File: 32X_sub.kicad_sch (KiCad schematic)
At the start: 98 parts, among them IC511 315-5684, IC512 315-5788, IC515 74HC74, IC516 74LS00, T520 TestPoint, T526 TestPoint, T527 TestPoint, T528 TestPoint, T547 TestPoint, T548 TestPoint, T555 TestPoint, T599 AS, X501 *3

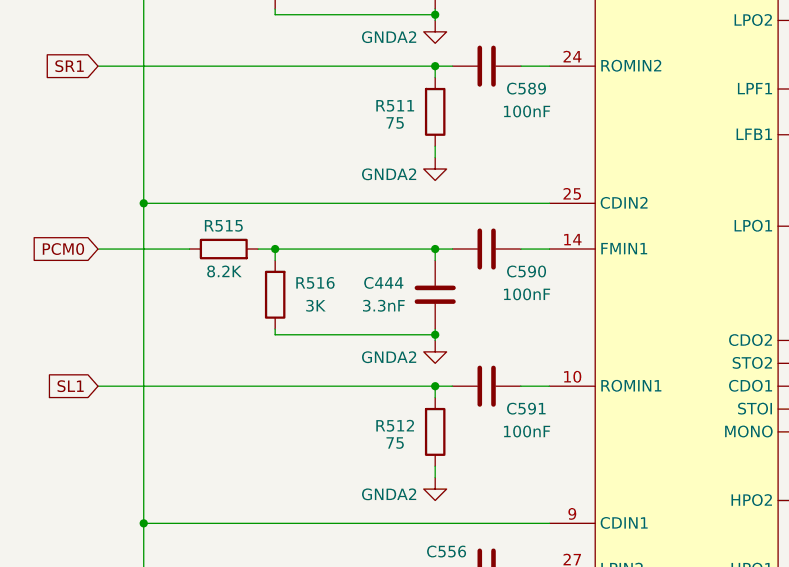
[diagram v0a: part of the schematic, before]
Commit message: BOM/footprint tweaks/corrections.
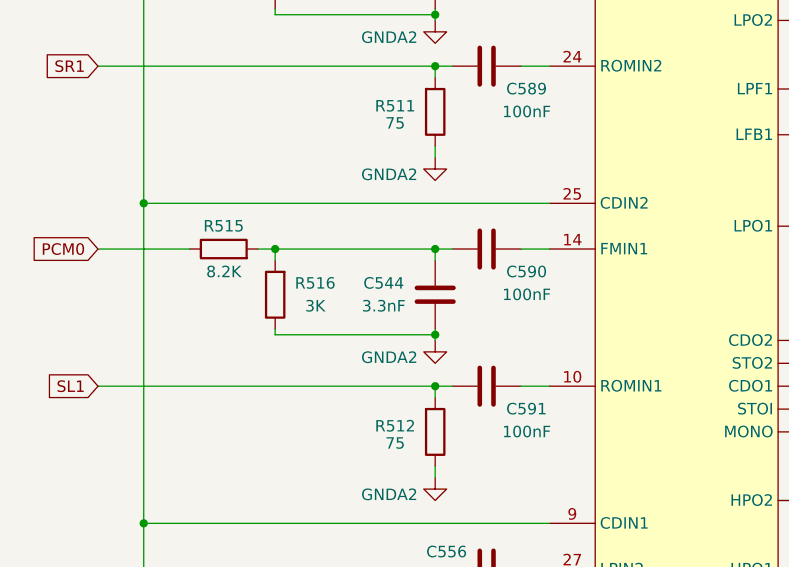
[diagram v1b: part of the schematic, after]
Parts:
- renumbered C444 to C544
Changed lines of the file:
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@@
   (symbol (lib_id "Device:C") (at 91.44 78.74 0) (mirror y) (unit 1)
     (in_bom yes) (on_board yes) (dnp no)
-    (property "Reference" "C444" (at 85.725 77.47 0)
+    (property "Reference" "C544" (at 85.725 77.47 0)
       (effects (font (size 1.27 1.27)))
     )
@@
       (project "Neptune"
         (path "/bcc23b51-b742-4ae5-9dd6-d96a24058944/edde10e2-ce08-4180-9fbe-ab298dfbfa4c"
-          (reference "C444") (unit 1)
+          (reference "C544") (unit 1)
         )
       )

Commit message: General tweaks, add some DigiKey part numbers.
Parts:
- CE17: DigiKey (none) -> 493-13447-1-ND
- R511, R512, R544: DigiKey (none) -> P75.0CCT-ND
- R525: DigiKey (none) -> P2.20KCCT-ND
- R826, R827, R828: DigiKey (none) -> P5.62KCCT-ND
- R829, R830, R831: DigiKey (none) -> P1.00KCCT-ND

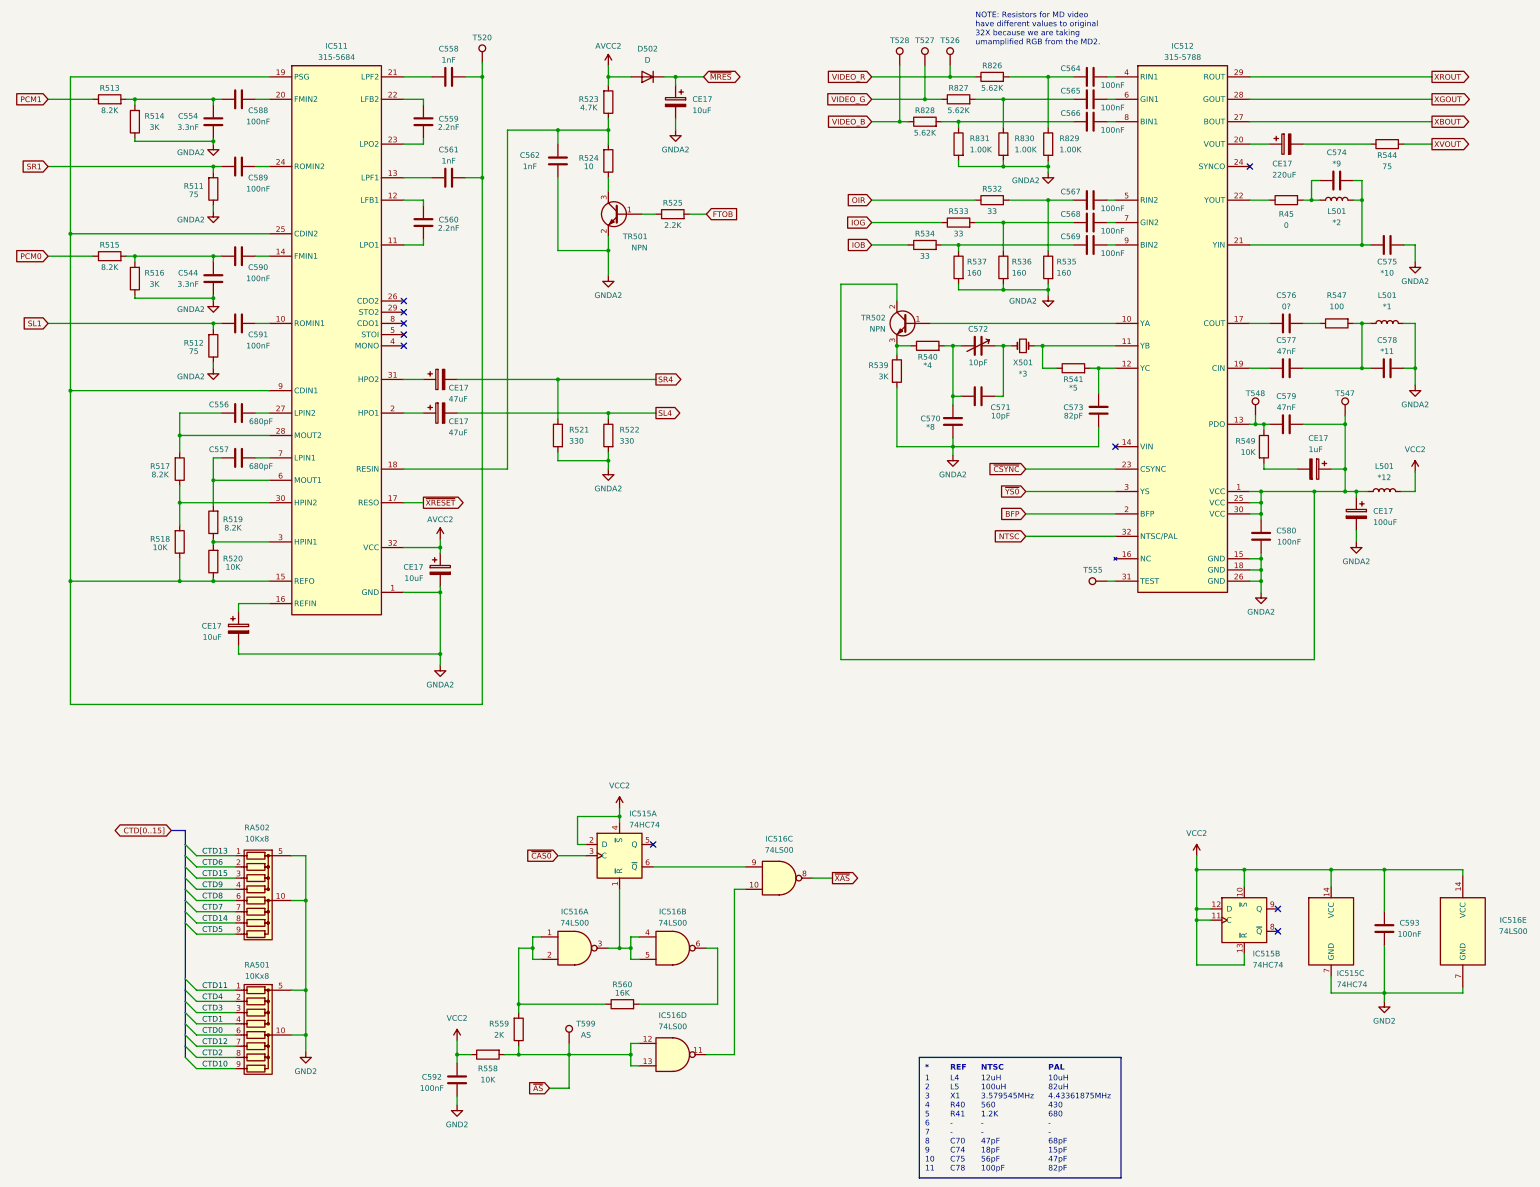
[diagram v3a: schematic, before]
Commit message: Apply fixes for issues found on prototype board.
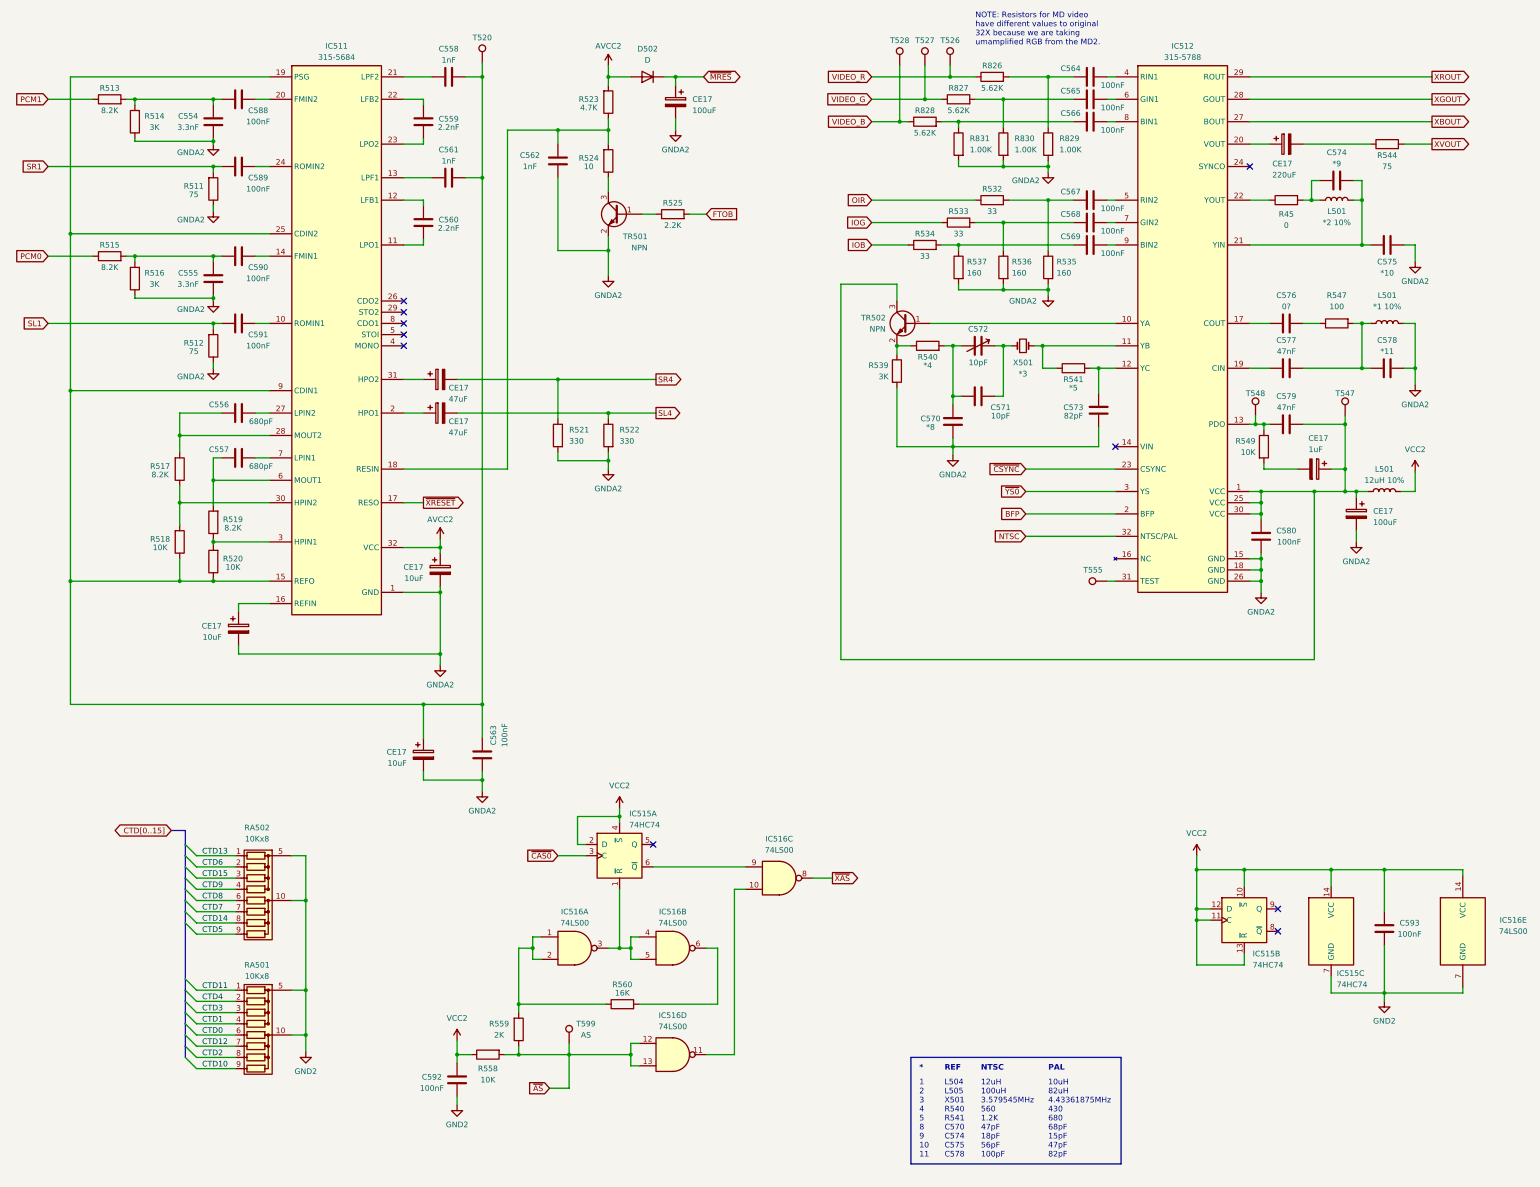
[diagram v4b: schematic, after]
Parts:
- added C563: 100nF, Capacitor_SMD:C_0805_2012Metric, symbol Device:C
- added CE17: 10uF, Capacitor_THT:CP_Radial_D5.0mm_P2.50mm, symbol Device:C_Polarized
- CE17: value 10uF -> 100uF
- L501: value *2 -> *2 10%; footprint Inductor_SMD:L_0805_2012Metric -> Inductor_SMD:L_1206_3216Metric
- L501: value *12 -> 12uH 10%; footprint Inductor_SMD:L_0805_2012Metric -> Inductor_SMD:L_1206_3216Metric
- L501: value *1 -> *1 10%; footprint Inductor_SMD:L_0805_2012Metric -> Inductor_SMD:L_1206_3216Metric
- TR502: symbol Device:Q_NPN_BCE -> Device:Q_NPN_BEC
- renumbered C544 to C555
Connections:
- net GNDA2: now also C563.1, CE17.2
- net at C558.2, C561.2, IC511.15 (REFO)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: now also C563.2, CE17.1
- net at C579.2, C580.2, CE17.1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: now also TR502.3 (C); no longer TR502.2 (C)
- net at R539.1, R540.1: now also TR502.2 (E); no longer TR502.3 (E)
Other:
- note added: "1 2 3 4 5 8 9 10 11"
- note added: "10uH 82uH 4.43361875MHz 430 680 68pF 15pF 47pF 82pF"
- note added: "12uH 100uH 3.579545MHz 560 1.2K 47pF 18pF 56pF 100pF"
- note added: "L504 L505 X501 R540 R541 C570 C574 C575 C578"
- note removed: "1 2 3 4 5 6 7 8 9 10 11"
- note removed: "10uH 82uH 4.43361875MHz 430 680 - - 68pF 15pF 47pF 82pF"
- note removed: "12uH 100uH 3.579545MHz 560 1.2K - - 47pF 18pF 56pF 100pF"
- note removed: "L4 L5 X1 R40 R41 - - C70 C74 C75 C78"

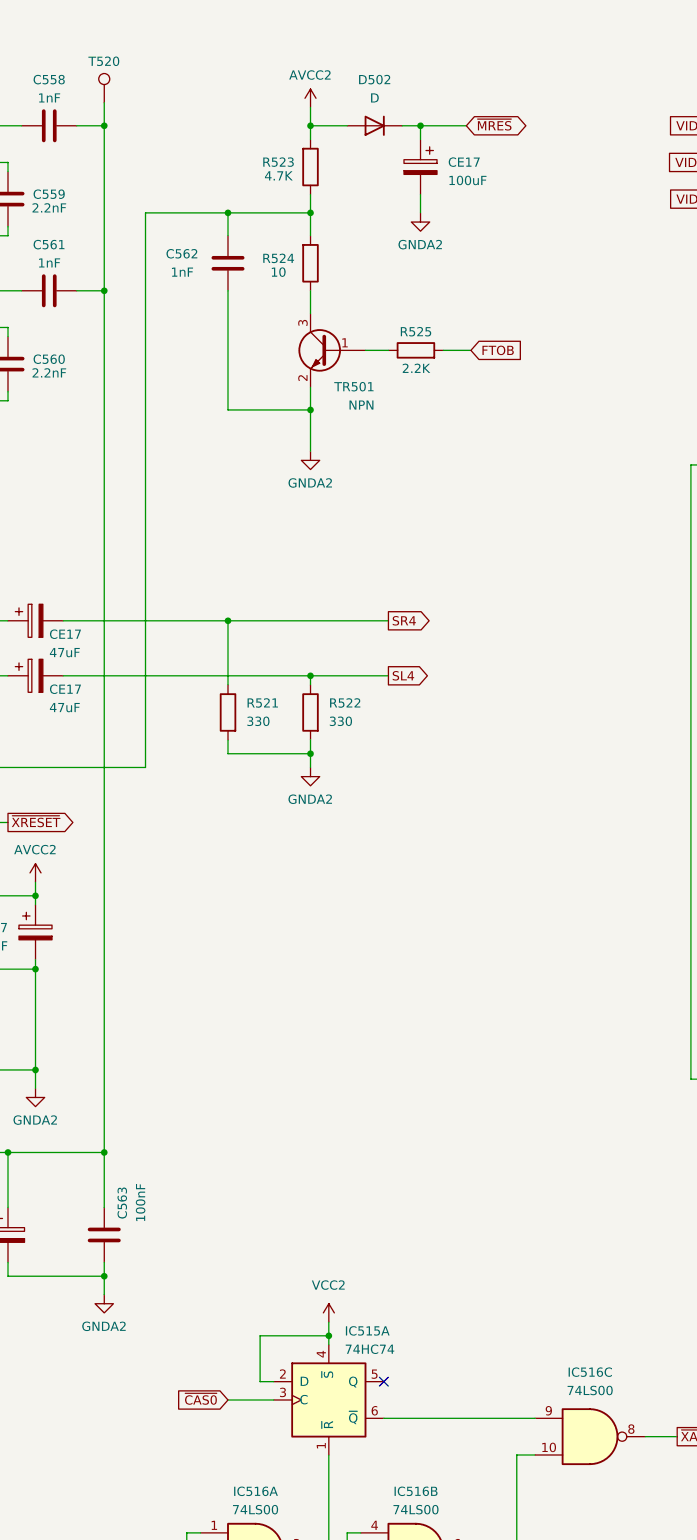
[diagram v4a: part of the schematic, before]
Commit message: Check through 32X VA0/VA1 differences/bodges.
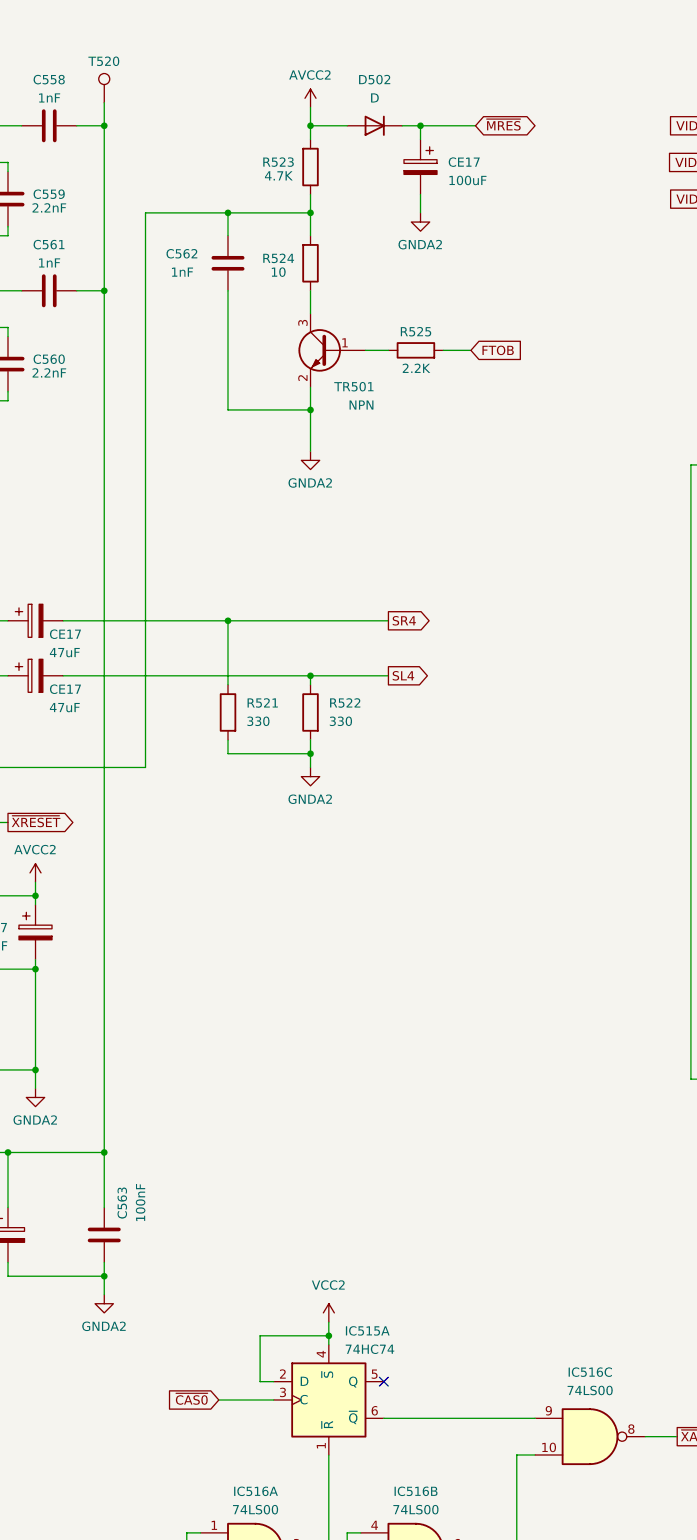
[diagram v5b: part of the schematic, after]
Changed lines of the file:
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@@
+    (stroke (width 0) (type default))
+  )
+  (wire (pts (xy 196.215 33.02) (xy 203.835 33.02))
     (stroke (width 0) (type default))
   )
@@
     (stroke (width 0) (type default))
   )
-  (wire (pts (xy 196.215 33.02) (xy 202.565 33.02))
-    (stroke (width 0) (type default))
-  )
   (wire (pts (xy 279.4 99.06) (xy 282.575 99.06))
     (stroke (width 0) (type default))
@@
     (stroke (width 0) (type default))
   )
+  (wire (pts (xy 196.215 42.545) (xy 196.215 45.085))
+    (stroke (width 0) (type default))
+  )
   (wire (pts (xy 356.87 240.665) (xy 344.805 240.665))
     (stroke (width 0) (type default))
@@
     (stroke (width 0) (type default))
   )
-  (wire (pts (xy 169.545 209.55) (xy 175.895 209.55))
-    (stroke (width 0) (type default))
-  )
   (wire (pts (xy 277.495 93.98) (xy 279.4 93.98))
     (stroke (width 0) (type default))
@@
     (stroke (width 0) (type default))
   )
-  (wire (pts (xy 196.215 42.545) (xy 196.215 45.085))
-    (stroke (width 0) (type default))
-  )
   (wire (pts (xy 100.965 38.1) (xy 104.14 38.1))
     (stroke (width 0) (type default))
@@
   )
   (wire (pts (xy 270.51 66.04) (xy 270.51 72.39))
+    (stroke (width 0) (type default))
+  )
+  (wire (pts (xy 168.275 209.55) (xy 175.895 209.55))
     (stroke (width 0) (type default))
   )
@@
     )
   )
-  (global_label "~{CAS0}" (shape input) (at 169.545 209.55 180) (fields_autoplaced)
-    (effects (font (size 1.27 1.27)) (justify right))
-    (property "Intersheetrefs" "${INTERSHEET_REFS}" (at 161.7822 209.55 0)
+  (global_label "~{CAS0}" (shape input) (at 168.275 209.55 180) (fields_autoplaced)
+    (effects (font (size 1.27 1.27)) (justify right))
+    (property "Intersheetrefs" "${INTERSHEET_REFS}" (at 160.5122 209.55 0)
       (effects (font (size 1.27 1.27)) (justify right) hide)
     )
@@
     )
   )
-  (global_label "~{MRES}" (shape bidirectional) (at 202.565 33.02 0) (fields_autoplaced)
+  (global_label "~{MRES}" (shape bidirectional) (at 203.835 33.02 0) (fields_autoplaced)
     (effects (font (size 1.27 1.27)) (justify left))
-    (property "Intersheetrefs" "${INTERSHEET_REFS}" (at 211.7414 33.02 0)
+    (property "Intersheetrefs" "${INTERSHEET_REFS}" (at 213.0114 33.02 0)
       (effects (font (size 1.27 1.27)) (justify left) hide)
     )

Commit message: Remove DRC warnings, update gerbers.
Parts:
- T520, T526, T527, T528, T547, T548, T555, T599: now left out of the parts list
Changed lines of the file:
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@@
   )
   (symbol (lib_id "Connector:TestPoint") (at 258.445 30.48 0) (unit 1)
-    (in_bom yes) (on_board yes) (dnp no)
+    (in_bom no) (on_board no) (dnp no)
     (property "Reference" "T526" (at 258.445 24.765 0)
       (effects (font (size 1.27 1.27)))
@@
       (effects (font (size 1.27 1.27)) hide)
     )
+    (property "Sim.Enable" "0" (at 258.445 30.48 0)
+      (effects (font (size 1.27 1.27)) hide)
+    )
     (pin "1")
     (instances
@@
   )
   (symbol (lib_id "Connector:TestPoint") (at 327.66 109.855 0) (unit 1)
-    (in_bom yes) (on_board yes) (dnp no)
+    (in_bom no) (on_board no) (dnp no)
     (property "Reference" "T548" (at 327.66 104.775 0)
       (effects (font (size 1.27 1.27)))
@@
       (effects (font (size 1.27 1.27)) hide)
     )
+    (property "Sim.Enable" "0" (at 327.66 109.855 0)
+      (effects (font (size 1.27 1.27)) hide)
+    )
     (pin "1")
     (instances
@@
   )
   (symbol (lib_id "Connector:TestPoint") (at 152.4 29.845 0) (unit 1)
-    (in_bom yes) (on_board yes) (dnp no)
+    (in_bom no) (on_board no) (dnp no)
     (property "Reference" "T520" (at 152.4 24.13 0)
       (effects (font (size 1.27 1.27)))
@@
       (effects (font (size 1.27 1.27)) hide)
     )
+    (property "Sim.Enable" "0" (at 152.4 29.845 0)
+      (effects (font (size 1.27 1.27)) hide)
+    )
     (pin "1")
     (instances
@@
   )
   (symbol (lib_id "Connector:TestPoint") (at 294.005 147.32 90) (unit 1)
-    (in_bom yes) (on_board yes) (dnp no)
+    (in_bom no) (on_board no) (dnp no)
     (property "Reference" "T555" (at 290.83 144.78 90)
       (effects (font (size 1.27 1.27)))
@@
       (effects (font (size 1.27 1.27)) hide)
     )
+    (property "Sim.Enable" "0" (at 294.005 147.32 0)
+      (effects (font (size 1.27 1.27)) hide)
+    )
     (pin "1")
     (instances
@@
   )
   (symbol (lib_id "Connector:TestPoint") (at 247.015 30.48 0) (unit 1)
-    (in_bom yes) (on_board yes) (dnp no)
+    (in_bom no) (on_board no) (dnp no)
     (property "Reference" "T528" (at 247.015 24.765 0)
       (effects (font (size 1.27 1.27)))
@@
       (effects (font (size 1.27 1.27)) hide)
     )
+    (property "Sim.Enable" "0" (at 247.015 30.48 0)
+      (effects (font (size 1.27 1.27)) hide)
+    )
     (pin "1")
     (instances
@@
   )
   (symbol (lib_id "Connector:TestPoint") (at 347.98 109.855 0) (unit 1)
-    (in_bom yes) (on_board yes) (dnp no)
+    (in_bom no) (on_board no) (dnp no)
     (property "Reference" "T547" (at 347.98 104.775 0)
       (effects (font (size 1.27 1.27)))
@@
       (effects (font (size 1.27 1.27)) hide)
     )
+    (property "Sim.Enable" "0" (at 347.98 109.855 0)
+      (effects (font (size 1.27 1.27)) hide)
+    )
     (pin "1")
     (instances
@@
   )
   (symbol (lib_id "Connector:TestPoint") (at 252.73 30.48 0) (unit 1)
-    (in_bom yes) (on_board yes) (dnp no)
+    (in_bom no) (on_board no) (dnp no)
     (property "Reference" "T527" (at 252.73 24.765 0)
       (effects (font (size 1.27 1.27)))
@@
       (effects (font (size 1.27 1.27)) hide)
     )
+    (property "Sim.Enable" "0" (at 252.73 30.48 0)
+      (effects (font (size 1.27 1.27)) hide)
+    )
     (pin "1")
     (instances
@@
   )
   (symbol (lib_id "Connector:TestPoint") (at 172.085 252.095 0) (unit 1)
-    (in_bom yes) (on_board yes) (dnp no)
+    (in_bom no) (on_board no) (dnp no)
     (property "Reference" "T599" (at 175.895 247.65 0)
       (effects (font (size 1.27 1.27)))
@@
       (effects (font (size 1.27 1.27)) hide)
     )
+    (property "Sim.Enable" "0" (at 172.085 252.095 0)
+      (effects (font (size 1.27 1.27)) hide)
+    )
